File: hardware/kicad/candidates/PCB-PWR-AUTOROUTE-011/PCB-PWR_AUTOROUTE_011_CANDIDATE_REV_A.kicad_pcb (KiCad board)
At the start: 4 copper layers, 90 x 60 mm, 66 parts, among them J1 43045-0213, J2 43045-1202, Q1 CSD18540Q5B, U1 LM74700QDBVRQ1, U2 INA226AIDGSR, U3 LMR604403SRAKR, U4 LMR604403SRAKR, U5 TPS7A2018PDBVR

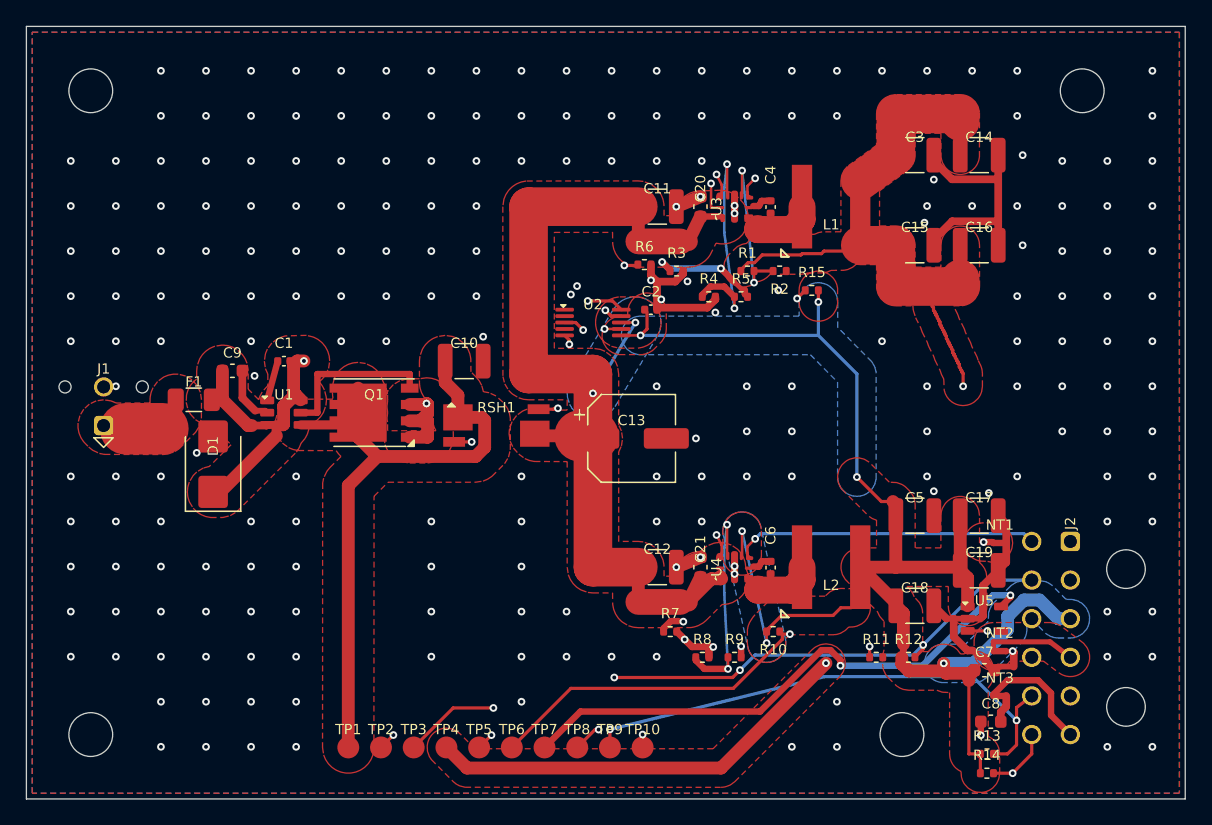
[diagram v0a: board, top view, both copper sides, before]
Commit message: apply: tools/apply_pcb_pwr_autoroute_candidate_rev_a.py
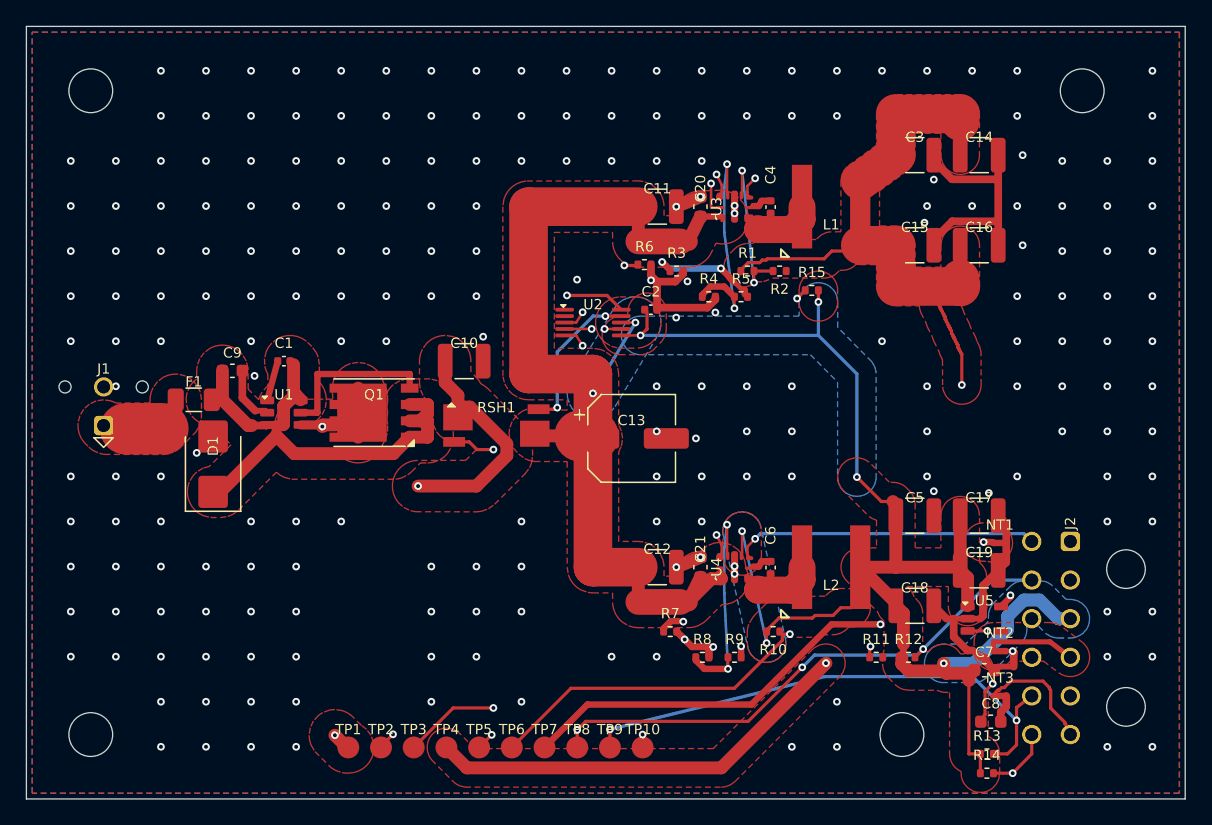
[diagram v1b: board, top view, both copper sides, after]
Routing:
- net I2C2_SDA: track 40.6 -> 75.8 mm, vias 2 -> 3
- net SHUNT_LOAD_SENSE: track 55.1 -> 44.8 mm
- net 1V8_MIC: track 68.4 -> 58.8 mm
- net VBAT_PROTECTED: track 52.6 -> 60.0 mm, vias 0 -> 3
- net SHUNT_SOURCE_SENSE: track 45.6 -> 49.1 mm
- net PG_3V8: track 65.1 -> 68.6 mm
- net I2C2_SCL: track 75.0 -> 73.9 mm
- net GND_MIC: track 9.31 -> 8.22 mm
- net VBAT_FUSED: track 41.2 -> 40.7 mm, vias 2 -> 0
- net FAULT: track 77.4 -> 77.0 mm, vias 5 -> 4
- net GND_PWR: vias 225 -> 224
- added copper zone on In2.Cu, net VBAT_PROTECTED
- removed copper zone on In2.Cu, net VBAT_FUSED

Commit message: apply: tools/apply_pcb_pwr_autoroute_candidate_rev_a.py
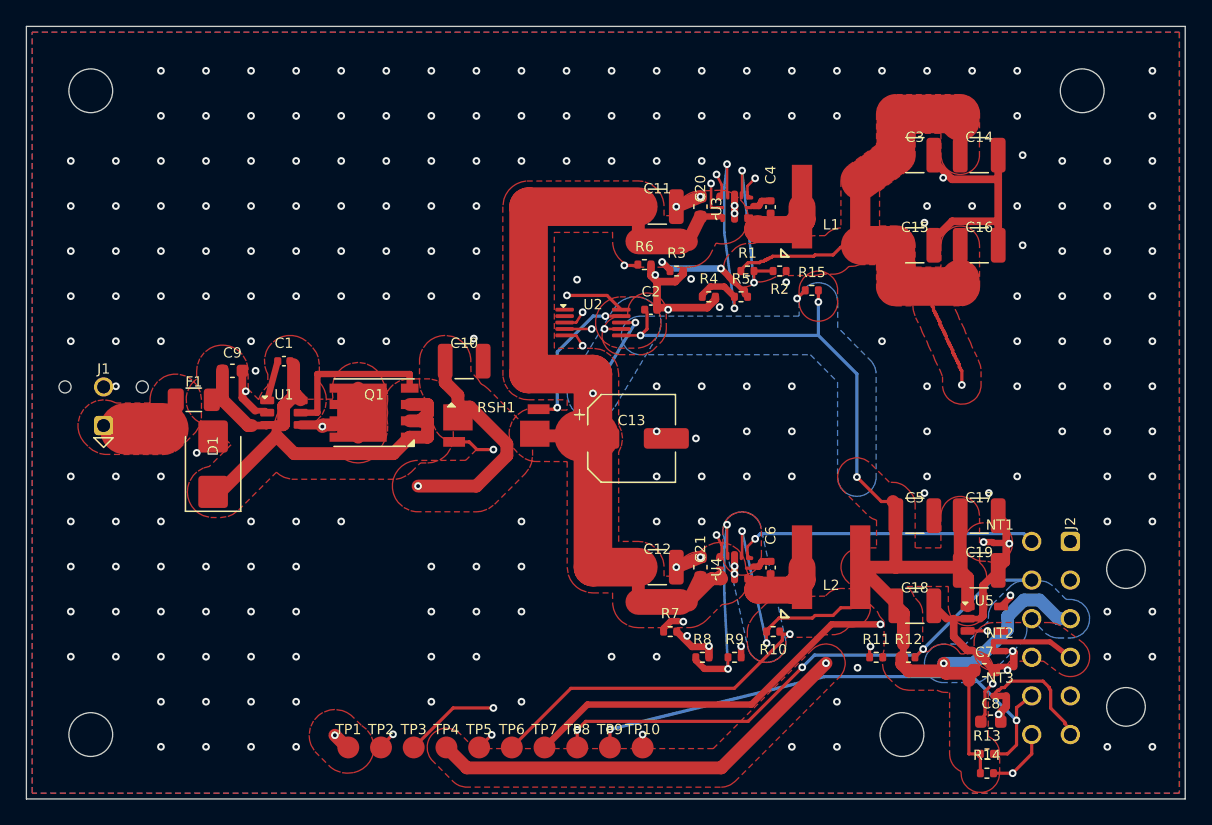
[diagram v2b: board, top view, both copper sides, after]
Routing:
- net 3V8_MODEM: track 117.2 -> 118.2 mm
- net GND_PWR: vias 224 -> 230

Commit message: apply: tools/apply_pcb_pwr_autoroute_candidate_rev_a.py
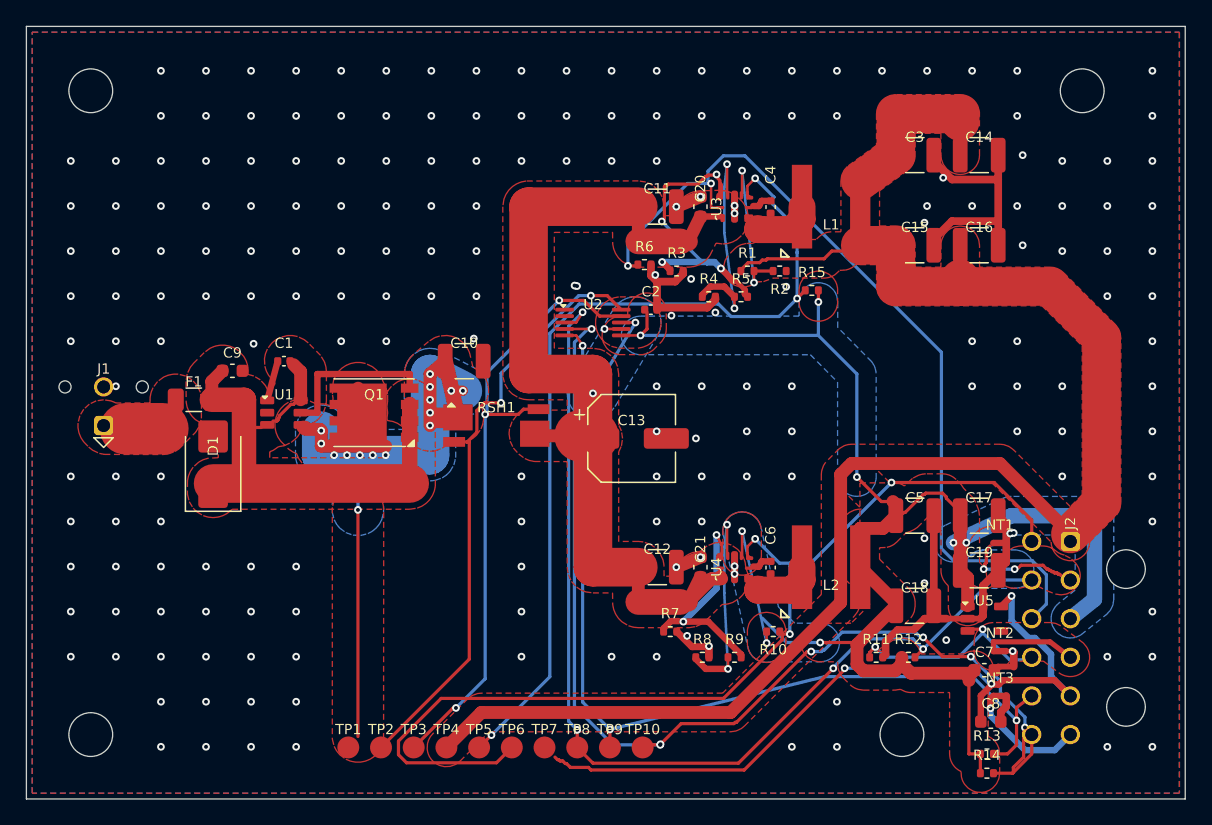
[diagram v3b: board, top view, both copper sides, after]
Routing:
- net 3V3_DIGITAL: track 114.0 -> 141.4 mm, vias 6 -> 8
- net PWR_GOOD: track 58.0 -> 80.0 mm, vias 2 -> 3
- net 3V8_MODEM: track 118.2 -> 137.3 mm, vias 2 -> 0
- net I2C2_SDA: track 75.8 -> 86.4 mm, vias 3 -> 7
- net RT_3V8: track 18.4 -> 24.6 mm, vias 3 -> 4
- net VBAT_PROTECTED: track 60.0 -> 64.5 mm, vias 3 -> 15
- net SHUNT_LOAD_SENSE: track 44.8 -> 49.2 mm
- net GND_PWR: track 68.8 -> 71.7 mm, vias 230 -> 207
- net FAULT: track 77.0 -> 79.7 mm
- net VBAT_FUSED: track 40.7 -> 42.9 mm
- net SHUNT_SOURCE_SENSE: track 49.1 -> 47.2 mm, vias 3 -> 2
- net GND_MIC: track 8.22 -> 9.44 mm, vias 0 -> 1
- net PG_3V8: track 68.6 -> 69.1 mm
- net RT_3V3: track 17.2 -> 17.6 mm, vias 3 -> 2
- net GND_MODEM: track 8.74 -> 8.46 mm, vias 1 -> 2
- added copper zone on B.Cu, net GND_MODEM
- added copper zone on In2.Cu, net GND_PWR
- added copper zone on B.Cu, net VBAT_PROTECTED
- removed copper zone on In2.Cu, net 3V8_MODEM
- removed copper zone on In2.Cu, net GND_MODEM
- removed copper zone on In2.Cu, net VBAT_PROTECTED

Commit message: apply: tools/apply_pcb_pwr_autoroute_candidate_rev_a.py
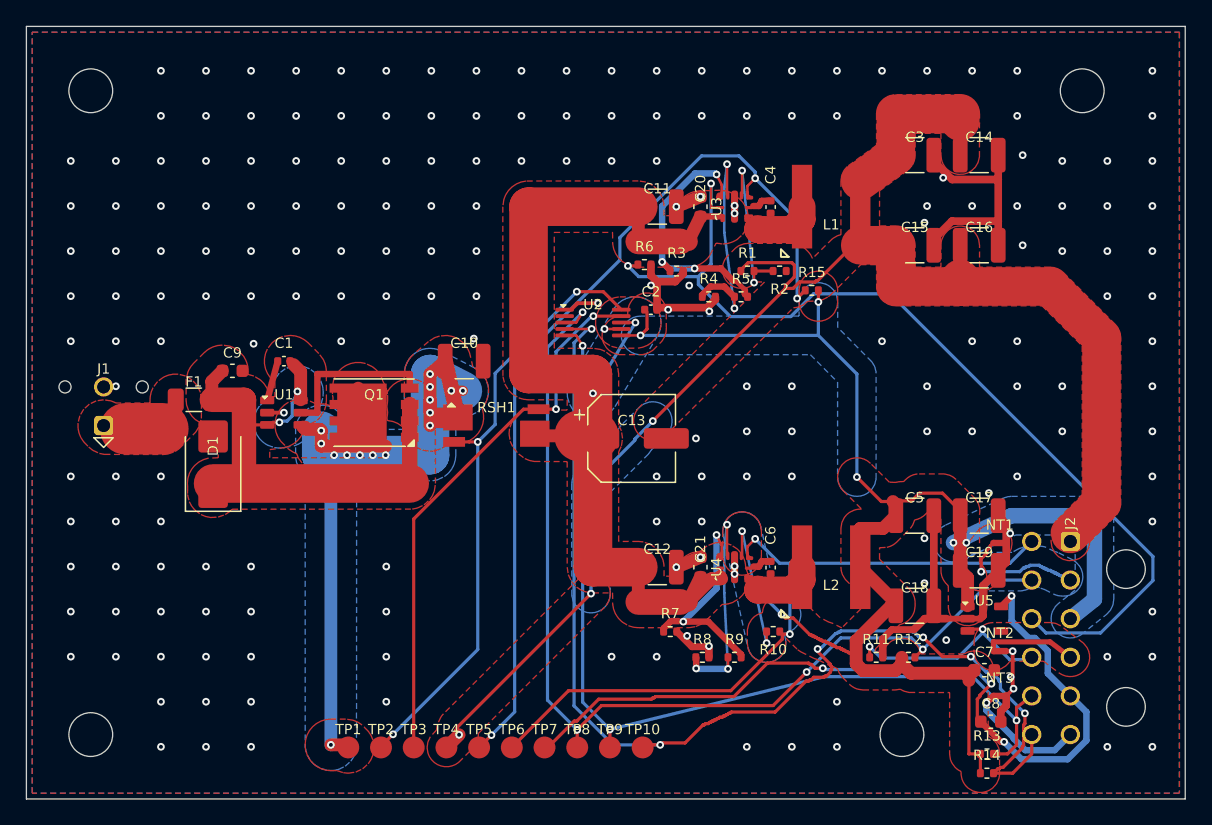
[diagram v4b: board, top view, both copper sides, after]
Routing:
- net PWR_GOOD: track 80.0 -> 56.1 mm, vias 3 -> 2
- net 3V8_MODEM: track 137.3 -> 122.0 mm, vias 0 -> 3
- net 3V3_DIGITAL: track 141.4 -> 128.5 mm
- net EN_MODEM: track 67.5 -> 76.4 mm
- net VBAT_PROTECTED: track 64.5 -> 70.8 mm
- net 1V8_MIC: track 59.2 -> 65.5 mm, vias 3 -> 4
- net SHUNT_LOAD_SENSE: track 49.2 -> 43.0 mm, vias 3 -> 2
- net GND_PWR: track 71.7 -> 76.3 mm, vias 207 -> 202
- net RT_3V8: track 24.6 -> 20.6 mm, vias 4 -> 3
- net I2C2_SDA: track 86.4 -> 89.6 mm, vias 7 -> 6
- net PG_3V8: track 69.1 -> 71.7 mm
- net GND_MODEM: track 8.46 -> 9.55 mm, vias 2 -> 1
- net VBAT_FUSED: track 42.9 -> 43.7 mm, vias 0 -> 2
- net MODE_3V3: track 17.5 -> 17.9 mm, vias 2 -> 3
- net SHUNT_SOURCE_SENSE: track 47.2 -> 47.6 mm, vias 2 -> 3
- added copper zone on B.Cu, net 3V8_MODEM
- added copper zone on B.Cu, net VBAT_FUSED

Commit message: apply: tools/apply_pcb_pwr_autoroute_candidate_rev_a.py
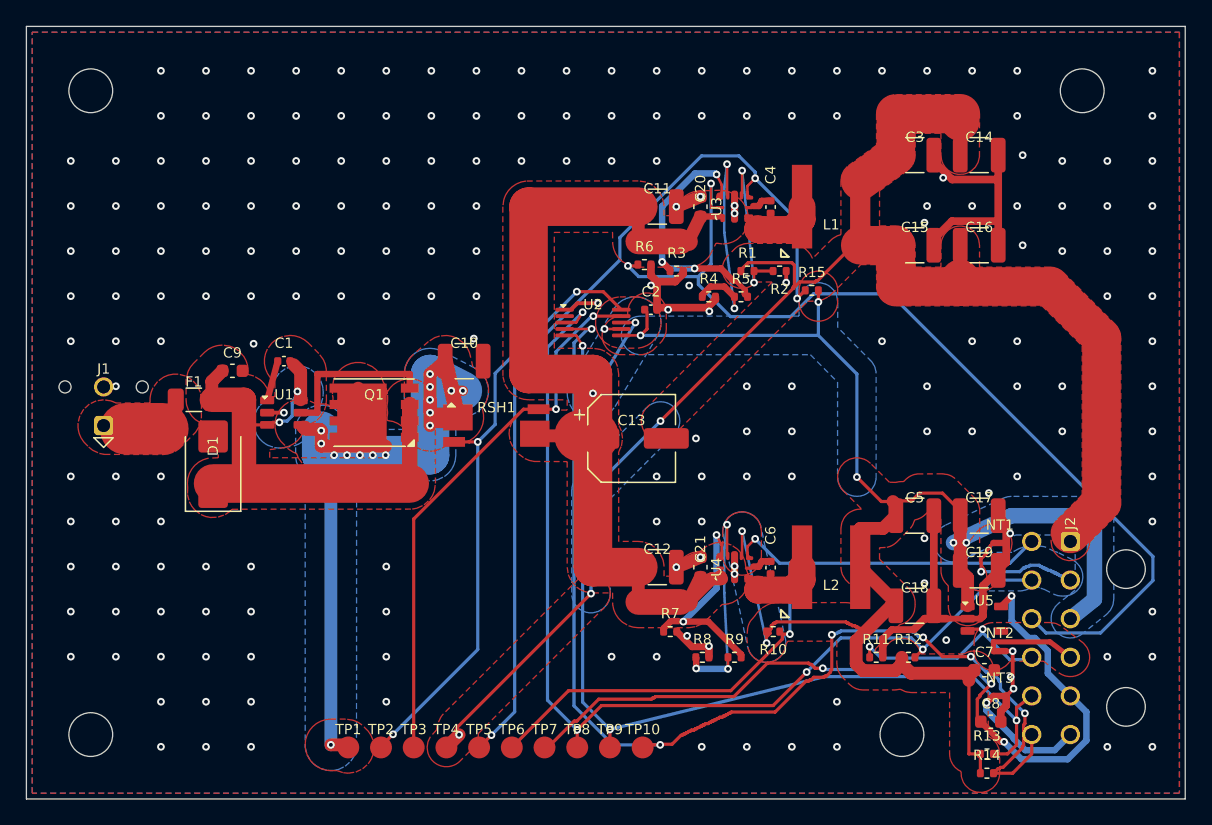
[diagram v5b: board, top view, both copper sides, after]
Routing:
- net 3V3_DIGITAL: track 128.5 -> 127.2 mm, vias 8 -> 7
- net I2C2_SDA: track 89.6 -> 88.7 mm
- net GND_PWR: track 76.3 -> 77.2 mm, vias 202 -> 204
- net 3V8_MODEM: track 122.0 -> 121.4 mm

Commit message: apply: tools/apply_pcb_pwr_autoroute_candidate_rev_a.py
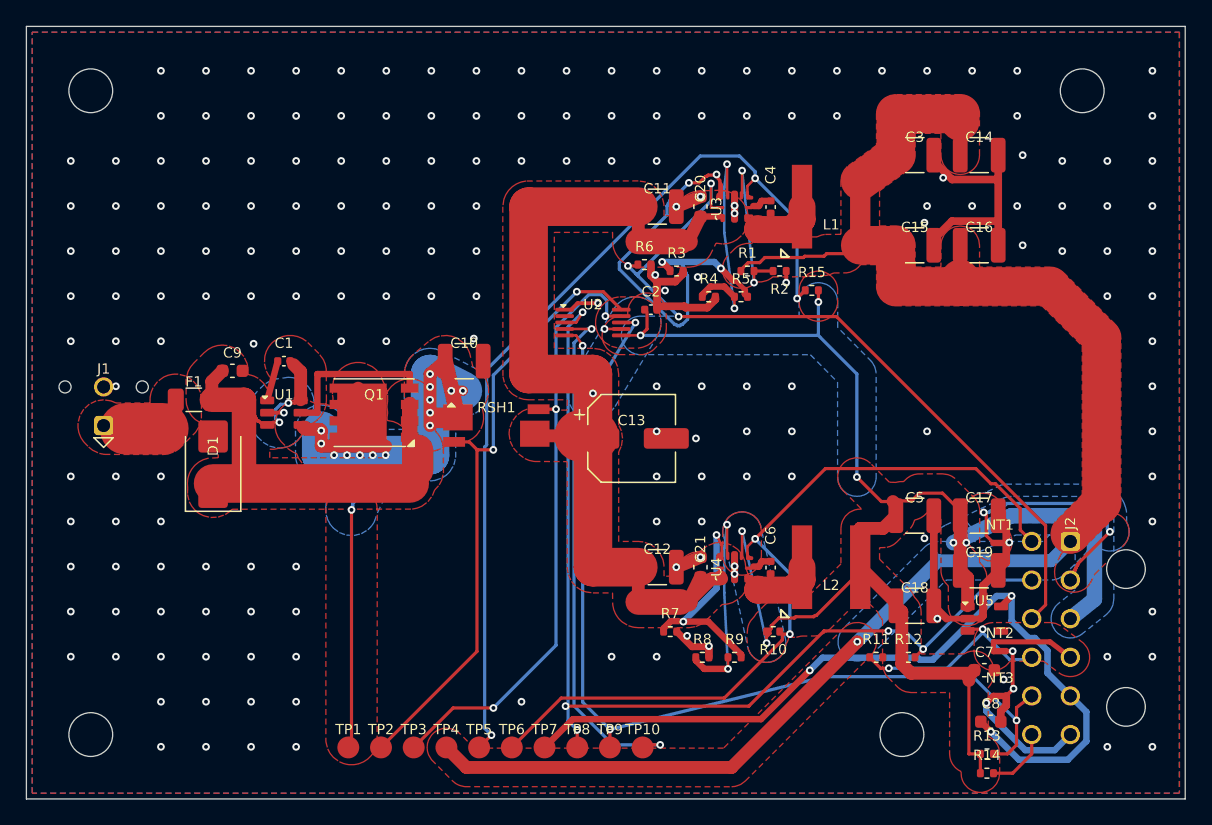
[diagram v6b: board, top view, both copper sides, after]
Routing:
- net I2C2_SDA: track 88.7 -> 46.6 mm, vias 6 -> 2
- net EN_MODEM: track 76.4 -> 61.3 mm, vias 2 -> 3
- net RT_3V8: track 20.6 -> 35.6 mm, vias 3 -> 4
- net 3V3_DIGITAL: track 127.2 -> 136.9 mm
- net GND_MODEM: track 9.55 -> 18.8 mm, vias 1 -> 2
- net PWR_GOOD: track 56.1 -> 63.2 mm
- net GND_PWR: track 77.2 -> 70.7 mm, vias 204 -> 192
- net 3V8_MODEM: track 121.4 -> 127.7 mm, vias 3 -> 1
- net VBAT_PROTECTED: track 70.8 -> 65.0 mm
- net SHUNT_LOAD_SENSE: track 43.0 -> 48.1 mm, vias 2 -> 3
- net VBAT_FUSED: track 43.7 -> 45.9 mm
- net 1V8_MIC: track 65.5 -> 66.4 mm, vias 4 -> 3
- net SHUNT_SOURCE_SENSE: track 47.6 -> 48.5 mm, vias 3 -> 2
- net FAULT: track 79.5 -> 78.9 mm, vias 4 -> 5
- net EN_AUX: track 17.0 -> 16.5 mm
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
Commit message: apply: tools/apply_pcb_pwr_autoroute_candidate_rev_a.py
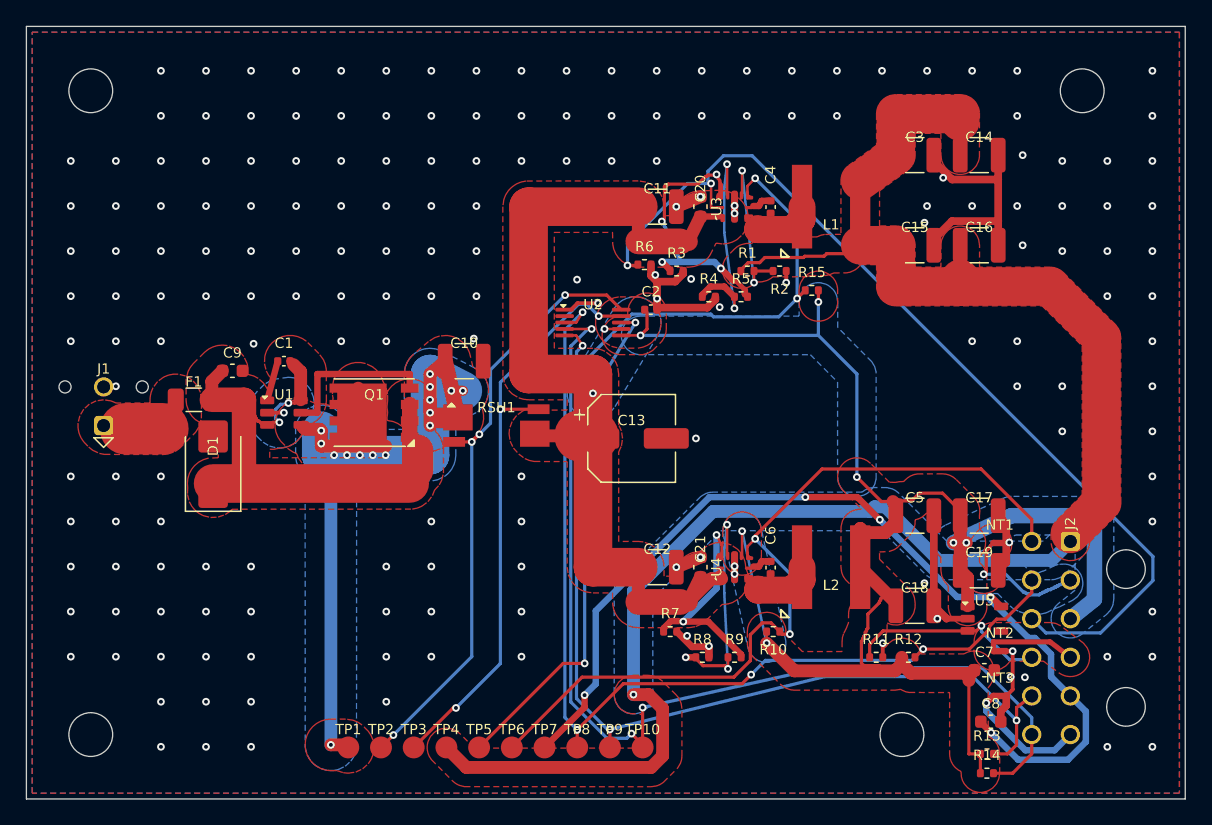
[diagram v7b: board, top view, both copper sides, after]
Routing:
- net I2C2_SDA: track 46.6 -> 81.1 mm, vias 2 -> 3
- net 3V8_MODEM: track 127.7 -> 143.1 mm
- net EN_MODEM: track 61.3 -> 75.9 mm, vias 3 -> 2
- net RT_3V8: track 35.6 -> 23.4 mm
- net 1V8_MIC: track 66.4 -> 75.5 mm, vias 3 -> 5
- net GND_MODEM: track 18.8 -> 9.93 mm, vias 2 -> 1
- net 3V3_DIGITAL: track 136.9 -> 130.3 mm
- net VBAT_PROTECTED: track 65.0 -> 70.8 mm
- net PG_3V8: track 72.2 -> 66.5 mm
- net GND_PWR: track 70.7 -> 66.4 mm, vias 192 -> 191
- net SHUNT_LOAD_SENSE: track 48.1 -> 46.5 mm
- net PWR_GOOD: track 63.2 -> 64.7 mm
- net SHUNT_SOURCE_SENSE: track 48.5 -> 47.3 mm, vias 2 -> 4
- net EN_AUX: track 16.5 -> 15.6 mm, vias 2 -> 1
- net FAULT: track 78.9 -> 78.3 mm, vias 5 -> 4
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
